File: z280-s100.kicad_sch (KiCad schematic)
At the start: 31 parts, among them J10 Config header (3x8), J7 Serial header (2x5), J8 S-100 edge connector (100-pin), J9 JTAG header (1x6), U1 Z280 Z-BUS (12 MHz), U10 AT28C256 (32Kx8), U11 AT28C256 (32Kx8), U12 LM7805, U13 DS1813, U14 MAX232, U15 74HCT245, U16 74HCT245, U17 74HCT245, U18 74HCT245, U19 74HCT245, U20 74HCT245, U21 74HCT244, U22 74F138, U23 74F521, U24 74F521, U4 ATF1508AS (PLCC-84), U5 ATF1508AS (PLCC-84), U6 IS61C5128AS-25 (512Kx8), U7 IS61C5128AS-25 (512Kx8), U8 IS61C5128AS-25 (512Kx8), U9 IS61C5128AS-25 (512Kx8), Y1 24 MHz

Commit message: Z280 S-100: buffer data bus (74F245), move A3-A15 latch out to 74HC573
The ATF1508 macrocell outputs can't meet the IEEE-696 24 mA data-bus sink
spec, so DO0-7 / DI0-7 now run through two 74F245 transceivers (64 mA sink).
DO_DIR / DI_DIR from the data CPLD drive their DIR pins; /OE is tied low
(a 245 in receive mode never drives the bus, so only DIR has to be right),
and both DIRs are DODSB-gated so a temporary master can float the drivers.

To free the two CPLD pins for those DIRs, the plain A3-A15 half of the
address demux latch moved back out to two 74HC573s (LATCH_LE = ~AS, /OE =
SLAVE); A0 (byte lane) and A1/A2 (burst counter) stay in the CPLD. The data
CPLD now fits at 53/64 I/O (was 64/64).

Also: the address 245s referenced stale LA1-15 nets while the CPLD drove
A1-15, leaving S-100 A1-A15 floating -- fixed. The redundant S100_DIR output
is gone; address/status/control 245 DIR is now wired straight to Z_BUSACK.

Co-Authored-By: Claude Code <noreply@anthropic.com>
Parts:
- added U2, U3: 74HC573, Package_DIP:DIP-20, symbol z280s100:74HC573
- added U25, U26: 74F245, Package_DIP:DIP-20, symbol z280s100:74F245
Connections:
- net LA1 is gone; now on net A1: U15.3 (A1)
- net LA10 is gone; now on net A10: U16.4 (A2)
- net LA11 is gone; now on net A11: U16.5 (A3)
- net LA12 is gone; now on net A12: U16.6 (A4)
- net LA13 is gone; now on net A13: U16.7 (A5)
- net LA14 is gone; now on net A14: U16.8 (A6)
- net LA15 is gone; now on net A15: U16.9 (A7)
- net LA2 is gone; now on net A2: U15.4 (A2)
- net LA3 is gone; now on net A3: U15.5 (A3)
- net LA4 is gone; now on net A4: U15.6 (A4)
- net LA5 is gone; now on net A5: U15.7 (A5)
- net LA6 is gone; now on net A6: U15.8 (A6)
- net LA7 is gone; now on net A7: U15.9 (A7)
- net LA8 is gone; now on net A8: U16.2 (A0)
- net LA9 is gone; now on net A9: U16.3 (A1)
- net +5V: now also U2.20 (+5V), U25.20 (+5V), U26.20 (+5V), U3.20 (+5V)
- net A10: now also U2.19 (Q7); no longer U5.33 (A10)
- net A11: now also U3.12 (Q0); no longer U5.34 (A11)
- net A12: now also U3.13 (Q1); no longer U5.35 (A12)
- net A13: now also U3.14 (Q2); no longer U5.36 (A13)
- net A14: now also U3.15 (Q3); no longer U5.37 (A14)
- net A15: now also U3.16 (Q4); no longer U5.39 (A15)
- net A3: now also U2.12 (Q0); no longer U5.24 (A3)
- net A4: now also U2.13 (Q1); no longer U5.25 (A4)
- net A5: now also U2.14 (Q2); no longer U5.27 (A5)
- net A6: now also U2.15 (Q3); no longer U5.28 (A6)
- net A7: now also U2.16 (Q4); no longer U5.29 (A7)
- net A8: now also U2.17 (Q5); no longer U5.30 (A8)
- net A9: now also U2.18 (Q6); no longer U5.31 (A9)
- net AD10: now also U2.9 (D7)
- net AD11: now also U3.2 (D0)
- net AD12: now also U3.3 (D1)
- net AD13: now also U3.4 (D2)
- net AD14: now also U3.5 (D3)
- net AD15: now also U3.6 (D4)
- net AD3: now also U2.2 (D0)
- net AD4: now also U2.3 (D1)
- net AD5: now also U2.4 (D2)
- net AD6: now also U2.5 (D3)
- net AD7: now also U2.6 (D4)
- net AD8: now also U2.7 (D5)
- net AD9: now also U2.8 (D6)
- net GND: now also U2.10 (GND), U25.10 (GND), U25.19 (OE), U26.10 (GND), U26.19 (OE), U3.10 (GND), U3.7 (D5), U3.8 (D6), U3.9 (D7)
- net S100_DI0: now also U26.11 (B0); no longer U5.73 (S100_DI0)
- net S100_DI1: now also U26.12 (B1); no longer U5.74 (S100_DI1)
- net S100_DI2: now also U26.13 (B2); no longer U5.75 (S100_DI2)
- net S100_DI3: now also U26.14 (B3); no longer U5.76 (S100_DI3)
- net S100_DI4: now also U26.15 (B4); no longer U5.77 (S100_DI4)
- net S100_DI5: now also U26.16 (B5); no longer U5.79 (S100_DI5)
- net S100_DI6: now also U26.17 (B6); no longer U5.80 (S100_DI6)
- net S100_DI7: now also U26.18 (B7); no longer U5.81 (S100_DI7)
- net S100_DO0: now also U25.11 (B0); no longer U5.61 (S100_DO0)
- net S100_DO1: now also U25.12 (B1); no longer U5.63 (S100_DO1)
- net S100_DO2: now also U25.13 (B2); no longer U5.64 (S100_DO2)
- net S100_DO3: now also U25.14 (B3); no longer U5.65 (S100_DO3)
- net S100_DO4: now also U25.15 (B4); no longer U5.67 (S100_DO4)
- net S100_DO5: now also U25.16 (B5); no longer U5.68 (S100_DO5)
- net S100_DO6: now also U25.17 (B6); no longer U5.69 (S100_DO6)
- net S100_DO7: now also U25.18 (B7); no longer U5.70 (S100_DO7)
- net SLAVE: now also U2.1 (OE), U3.1 (OE)
- net Z_BUSACK: now also U15.1 (DIR), U16.1 (DIR), U17.1 (DIR), U18.1 (DIR), U19.1 (DIR)
- removed net S100_DIR: U15.1 (DIR), U16.1 (DIR), U17.1 (DIR), U18.1 (DIR), U19.1 (DIR), U5.6 (S100_DIR)
- new net CPLD_DI0: U26.2 (A0), U5.73 (CPLD_DI0)
- new net CPLD_DI1: U26.3 (A1), U5.74 (CPLD_DI1)
- new net CPLD_DI2: U26.4 (A2), U5.75 (CPLD_DI2)
- new net CPLD_DI3: U26.5 (A3), U5.76 (CPLD_DI3)
- new net CPLD_DI4: U26.6 (A4), U5.77 (CPLD_DI4)
- new net CPLD_DI5: U26.7 (A5), U5.79 (CPLD_DI5)
- new net CPLD_DI6: U26.8 (A6), U5.80 (CPLD_DI6)
- new net CPLD_DI7: U26.9 (A7), U5.81 (CPLD_DI7)
- new net CPLD_DO0: U25.2 (A0), U5.61 (CPLD_DO0)
- new net CPLD_DO1: U25.3 (A1), U5.63 (CPLD_DO1)
- new net CPLD_DO2: U25.4 (A2), U5.64 (CPLD_DO2)
- new net CPLD_DO3: U25.5 (A3), U5.65 (CPLD_DO3)
- new net CPLD_DO4: U25.6 (A4), U5.67 (CPLD_DO4)
- new net CPLD_DO5: U25.7 (A5), U5.68 (CPLD_DO5)
- new net CPLD_DO6: U25.8 (A6), U5.69 (CPLD_DO6)
- new net CPLD_DO7: U25.9 (A7), U5.70 (CPLD_DO7)
- new net DI_DIR: U26.1 (DIR), U5.25 (DI_DIR)
- new net DO_DIR: U25.1 (DIR), U5.24 (DO_DIR)
- new net LATCH_LE: U2.11 (LE), U3.11 (LE), U5.6 (LATCH_LE)

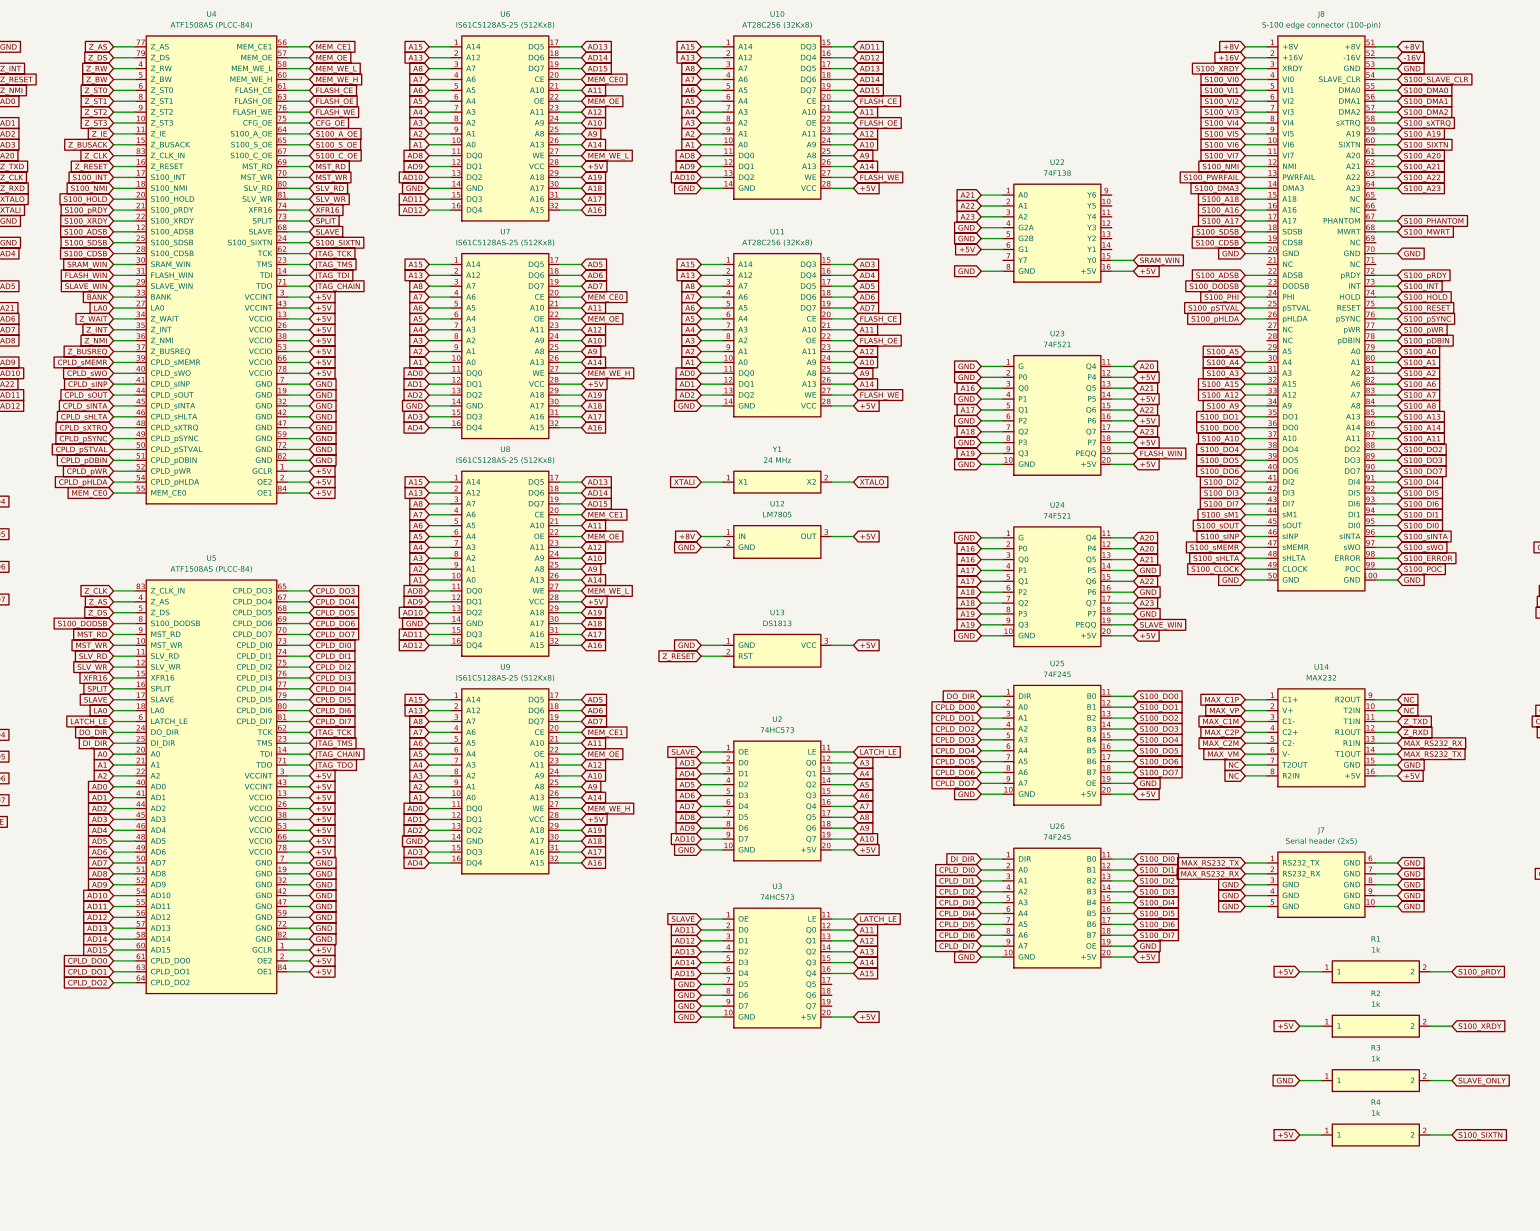
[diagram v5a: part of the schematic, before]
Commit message: Z280 S-100: deterministic schematic UUIDs; unify S-100 footprint name
uid() now derives each schematic UUID from a stable identity key (uuid5) instead of uuid4, so regenerating the schematic no longer churns symbol UUIDs; the board's footprint (path ...) links survive Update PCB from Schematic.

S-100 edge connector footprint unified on S100_MALE (the schematic carried a phantom Connector_Edge that broke net updates). Sync U27/Y2/U13/J7 positions from the schematic; regenerate the netlist and update the board's 42 footprint path UUIDs to match.

Also rename decode signal BANK -> A20 and convert DIP/header placements to library footprints in gen_pcb.py.

Co-Authored-By: Claude Code <noreply@anthropic.com>
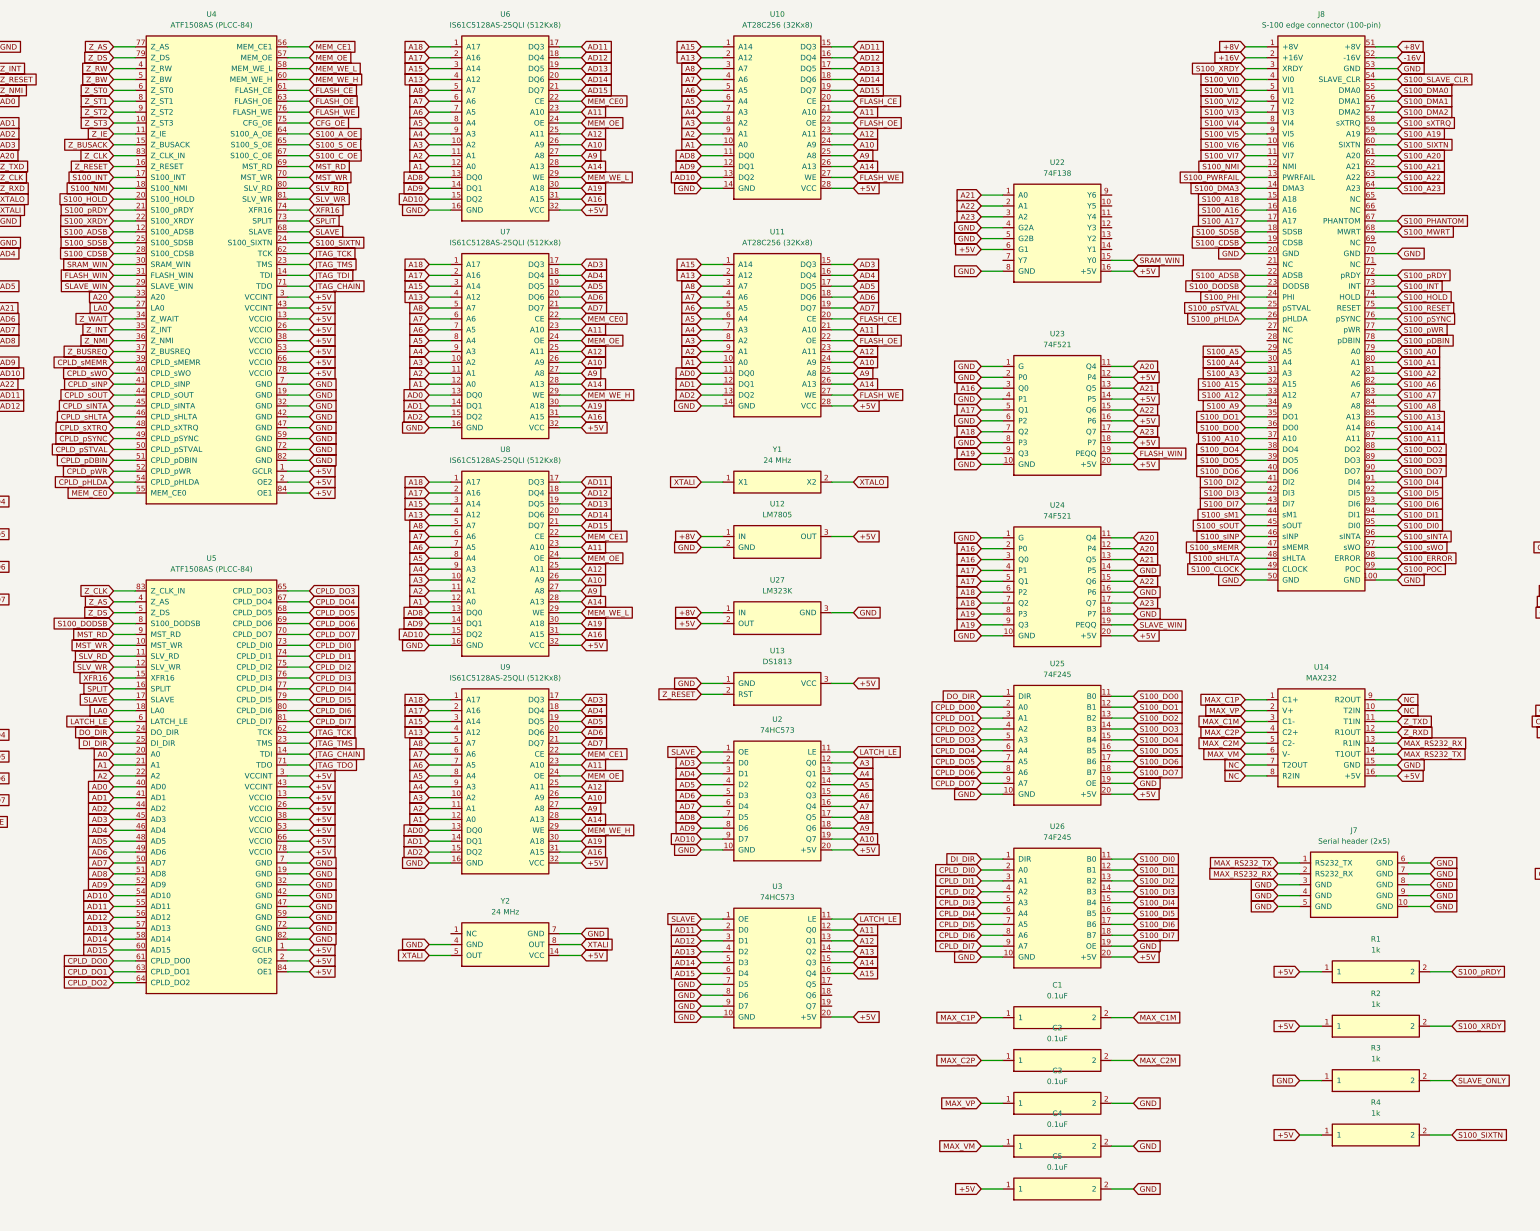
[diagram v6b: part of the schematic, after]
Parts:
- added C1, C2, C3, C4, C5: 0.1uF, Capacitor_THT:C_Disc_D5.0mm_W2.5mm_P2.50mm, symbol z280s100:C
- added U27: LM323K, Package_TO_SOT_THT:TO-3, symbol z280s100:LM323K
- added Y2: 24 MHz, z280-s100:Oscillator_DIP-8-14, symbol z280s100:Oscillator
- J8: footprint Connector_Edge -> S100_MALE
- U12: footprint Package_TO_SOT:TO-220-3 -> Package_TO_SOT_THT:TO-220-3_Horizontal_TabDown
- U13: footprint Package_TO_SOT:TO-92 -> Package_TO_SOT_THT:TO-92_Inline
- U14, U22: footprint Package_DIP:DIP-16 -> Package_DIP:DIP-16_W7.62mm
- U15, U16, U17, U18, U19, U2, U20, U21, U23, U24, U25, U26, U3: footprint Package_DIP:DIP-20 -> Package_DIP:DIP-20_W7.62mm
- U6, U7, U8, U9: value IS61C5128AS-25 (512Kx8) -> IS61C5128AS-25QLI (512Kx8); footprint Package_DIP:DIP-32 -> Package_DIP:DIP-32_W15.24mm
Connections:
- net BANK is gone; now on net A20: U4.33 (A20)
- net +5V: now also U6.32 (VCC), U7.32 (VCC), U8.32 (VCC), U9.32 (VCC), C5.1, U27.2 (OUT), Y2.14 (VCC); no longer U6.28 (VCC), U7.28 (VCC), U8.28 (VCC), U9.28 (VCC)
- net +8V: now also U27.1 (IN)
- net A1: now also U6.12 (A0), U7.12 (A0), U8.12 (A0), U9.12 (A0); no longer U6.10 (A0), U7.10 (A0), U8.10 (A0), U9.10 (A0)
- net A10: now also U6.26 (A9), U7.26 (A9), U8.26 (A9), U9.26 (A9); no longer U6.24 (A9), U7.24 (A9), U8.24 (A9), U9.24 (A9)
- net A11: now also U6.23 (A10), U7.23 (A10), U8.23 (A10), U9.23 (A10); no longer U6.21 (A10), U7.21 (A10), U8.21 (A10), U9.21 (A10)
- net A12: now also U6.25 (A11), U7.25 (A11), U8.25 (A11), U9.25 (A11); no longer U6.23 (A11), U7.23 (A11), U8.23 (A11), U9.23 (A11)
- net A13: now also U6.4 (A12), U7.4 (A12), U8.4 (A12), U9.4 (A12); no longer U6.2 (A12), U7.2 (A12), U8.2 (A12), U9.2 (A12)
- net A14: now also U6.28 (A13), U7.28 (A13), U8.28 (A13), U9.28 (A13); no longer U6.26 (A13), U7.26 (A13), U8.26 (A13), U9.26 (A13)
- net A15: now also U6.3 (A14), U7.3 (A14), U8.3 (A14), U9.3 (A14); no longer U6.1 (A14), U7.1 (A14), U8.1 (A14), U9.1 (A14)
- net A16: now also U6.31 (A15), U7.31 (A15), U8.31 (A15), U9.31 (A15); no longer U6.32 (A15), U7.32 (A15), U8.32 (A15), U9.32 (A15)
- net A17: now also U6.2 (A16), U7.2 (A16), U8.2 (A16), U9.2 (A16); no longer U6.31 (A16), U7.31 (A16), U8.31 (A16), U9.31 (A16)
- net A18: now also U6.1 (A17), U7.1 (A17), U8.1 (A17), U9.1 (A17); no longer U6.30 (A17), U7.30 (A17), U8.30 (A17), U9.30 (A17)
- net A19: now also U6.30 (A18), U7.30 (A18), U8.30 (A18), U9.30 (A18); no longer U6.29 (A18), U7.29 (A18), U8.29 (A18), U9.29 (A18)
- net A2: now also U6.11 (A1), U7.11 (A1), U8.11 (A1), U9.11 (A1); no longer U6.9 (A1), U7.9 (A1), U8.9 (A1), U9.9 (A1)
- net A3: now also U6.10 (A2), U7.10 (A2), U8.10 (A2), U9.10 (A2); no longer U6.8 (A2), U7.8 (A2), U8.8 (A2), U9.8 (A2)
- net A4: now also U6.9 (A3), U7.9 (A3), U8.9 (A3), U9.9 (A3); no longer U6.7 (A3), U7.7 (A3), U8.7 (A3), U9.7 (A3)
- net A5: now also U6.8 (A4), U7.8 (A4), U8.8 (A4), U9.8 (A4); no longer U6.6 (A4), U7.6 (A4), U8.6 (A4), U9.6 (A4)
- net A6: now also U6.7 (A5), U7.7 (A5), U8.7 (A5), U9.7 (A5); no longer U6.5 (A5), U7.5 (A5), U8.5 (A5), U9.5 (A5)
- net A7: now also U6.6 (A6), U7.6 (A6), U8.6 (A6), U9.6 (A6); no longer U6.4 (A6), U7.4 (A6), U8.4 (A6), U9.4 (A6)
- net A8: now also U6.5 (A7), U7.5 (A7), U8.5 (A7), U9.5 (A7); no longer U6.3 (A7), U7.3 (A7), U8.3 (A7), U9.3 (A7)
- net A9: now also U6.27 (A8), U7.27 (A8), U8.27 (A8), U9.27 (A8); no longer U6.25 (A8), U7.25 (A8), U8.25 (A8), U9.25 (A8)
- net AD0: now also U7.13 (DQ0), U9.13 (DQ0); no longer U7.11 (DQ0), U9.11 (DQ0)
- net AD1: now also U7.14 (DQ1), U9.14 (DQ1); no longer U7.12 (DQ1), U9.12 (DQ1)
- net AD10: now also U6.15 (DQ2), U8.15 (DQ2); no longer U6.13 (DQ2), U8.13 (DQ2)
- net AD11: now also U6.17 (DQ3), U8.17 (DQ3); no longer U6.15 (DQ3), U8.15 (DQ3)
- net AD12: now also U6.18 (DQ4), U8.18 (DQ4); no longer U6.16 (DQ4), U8.16 (DQ4)
- net AD13: now also U6.19 (DQ5), U8.19 (DQ5); no longer U6.17 (DQ5), U8.17 (DQ5)
- net AD14: now also U6.20 (DQ6), U8.20 (DQ6); no longer U6.18 (DQ6), U8.18 (DQ6)
- net AD15: now also U6.21 (DQ7), U8.21 (DQ7); no longer U6.19 (DQ7), U8.19 (DQ7)
- net AD2: now also U7.15 (DQ2), U9.15 (DQ2); no longer U7.13 (DQ2), U9.13 (DQ2)
- net AD3: now also U7.17 (DQ3), U9.17 (DQ3); no longer U7.15 (DQ3), U9.15 (DQ3)
- net AD4: now also U7.18 (DQ4), U9.18 (DQ4); no longer U7.16 (DQ4), U9.16 (DQ4)
- net AD5: now also U7.19 (DQ5), U9.19 (DQ5); no longer U7.17 (DQ5), U9.17 (DQ5)
- net AD6: now also U7.20 (DQ6), U9.20 (DQ6); no longer U7.18 (DQ6), U9.18 (DQ6)
- net AD7: now also U7.21 (DQ7), U9.21 (DQ7); no longer U7.19 (DQ7), U9.19 (DQ7)
- net AD8: now also U6.13 (DQ0), U8.13 (DQ0); no longer U6.11 (DQ0), U8.11 (DQ0)
- net AD9: now also U6.14 (DQ1), U8.14 (DQ1); no longer U6.12 (DQ1), U8.12 (DQ1)
- net GND: now also U6.16 (GND), U7.16 (GND), U8.16 (GND), U9.16 (GND), C3.2, C4.2, C5.2, U27.3 (GND), Y2.4 (GND), Y2.7 (GND); no longer U6.14 (GND), U7.14 (GND), U8.14 (GND), U9.14 (GND)
- net MAX_C1M: now also C1.2
- net MAX_C1P: now also C1.1
- net MAX_C2M: now also C2.2
- net MAX_C2P: now also C2.1
- net MAX_VM: now also C4.1
- net MAX_VP: now also C3.1
- net MEM_CE0: now also U6.22 (CE), U7.22 (CE); no longer U6.20 (CE), U7.20 (CE)
- net MEM_CE1: now also U8.22 (CE), U9.22 (CE); no longer U8.20 (CE), U9.20 (CE)
- net MEM_OE: now also U6.24 (OE), U7.24 (OE), U8.24 (OE), U9.24 (OE); no longer U6.22 (OE), U7.22 (OE), U8.22 (OE), U9.22 (OE)
- net MEM_WE_H: now also U7.29 (WE), U9.29 (WE); no longer U7.27 (WE), U9.27 (WE)
- net MEM_WE_L: now also U6.29 (WE), U8.29 (WE); no longer U6.27 (WE), U8.27 (WE)
- net XTALI: now also Y2.5 (OUT), Y2.8 (OUT)
